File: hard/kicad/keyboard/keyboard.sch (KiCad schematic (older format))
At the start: 91 parts, among them SW01 Space, SW02 <, SW04 Tab, SW08 º \\, SW101 Space, SW11 Z, SW12 A, SW14 Q, SW18 1, SW1F1 Alt, SW1F2 Control, SW1F4 Shift, SW201 Space, SW21 X, SW22 S, SW24 W, SW28 2, SW31 C, SW32 D, SW34 E, SW38 3, SW41 V, SW42 F, SW44 R, SW48 4, SW51 B, SW52 G, SW54 T, SW58 5, SW61 N, SW62 H, SW64 Y, SW68 6, SW71 M, SW72 J, SW74 U, SW78 7, SW81 ,, SW82 K, SW84 I, SW88 8, SW91 ., SW92 L, SW94 O, SW98 9, U1 74HC154

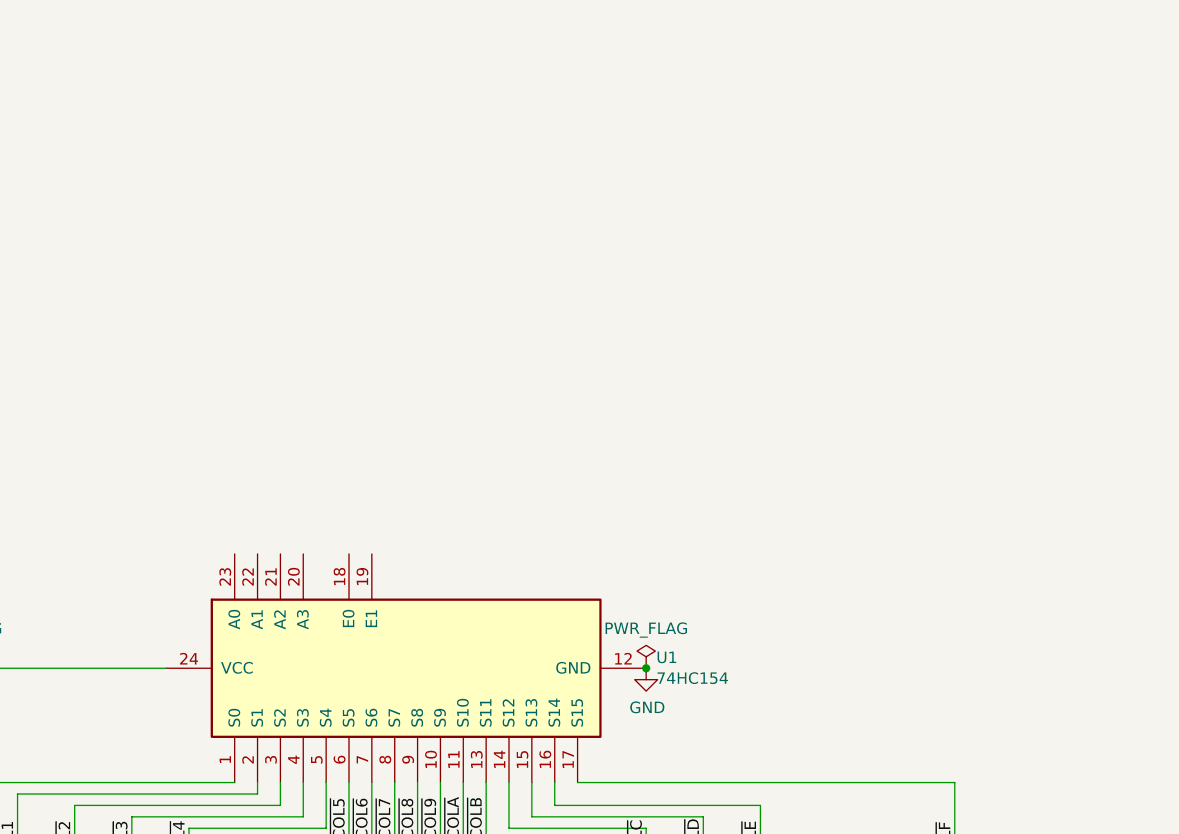
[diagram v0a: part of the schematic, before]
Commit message: update ASCII keyboard
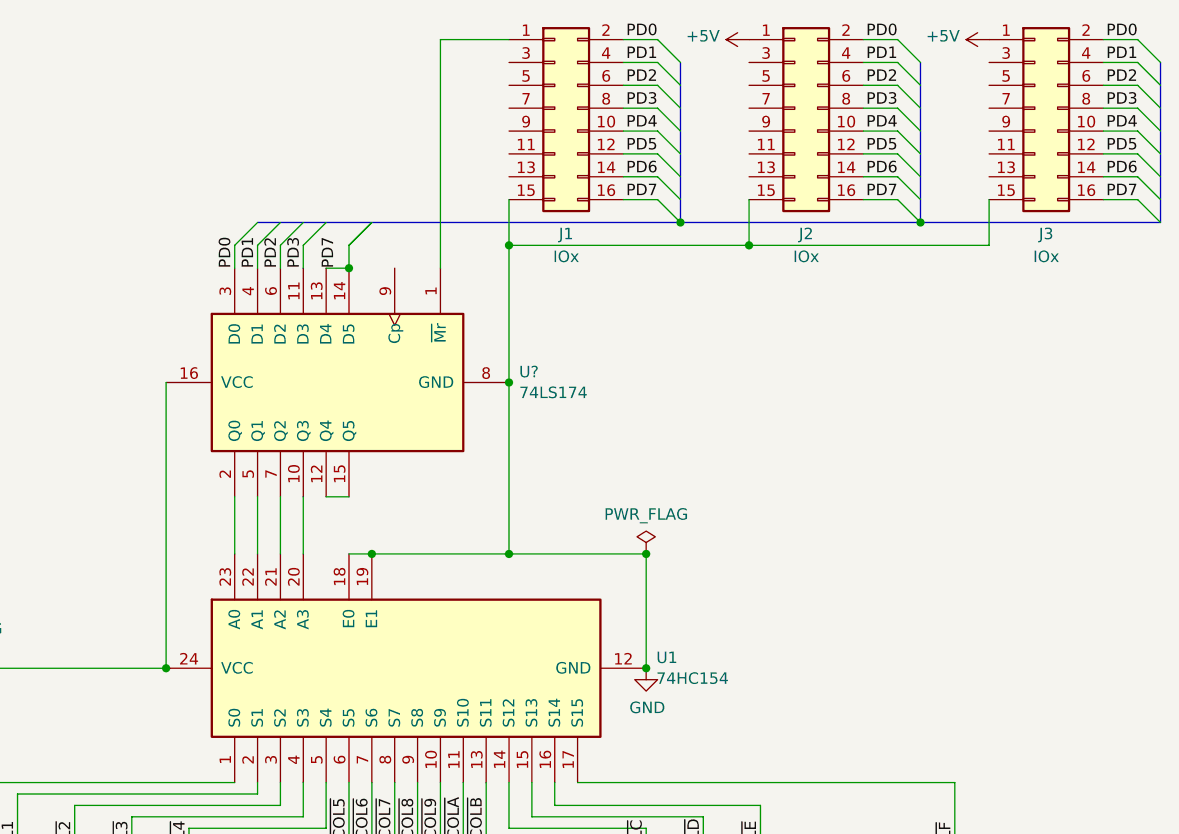
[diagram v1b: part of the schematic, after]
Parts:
- added J1, J2, J3: IOx, symbol Connector_Generic:Conn_02x08_Odd_Even
- added U?: 74LS174, symbol 74xx:74LS174
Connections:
- net +5V: now also J2.1 (Pin_1), J3.1 (Pin_1), U?.16 (VCC)
- net GND: now also U1.18 (E0), U1.19 (E1), J1.15 (Pin_15), J2.15 (Pin_15), J3.15 (Pin_15), U?.8 (GND)
- net at U1.20 (A3): now also U?.10 (Q3)
- net at U1.21 (A2): now also U?.7 (Q2)
- net at U1.22 (A1): now also U?.5 (Q1)
- net at U1.23 (A0): now also U?.2 (Q0)
- new net: J1.1 (Pin_1), U?.1 (~Mr)
- new net: U?.12 (Q4), U?.15 (Q5)
- new net PD0: J1.2 (Pin_2), J2.2 (Pin_2), J3.2 (Pin_2), U?.3 (D0)
- new net PD1: J1.4 (Pin_4), J2.4 (Pin_4), J3.4 (Pin_4), U?.4 (D1)
- new net PD2: J1.6 (Pin_6), J2.6 (Pin_6), J3.6 (Pin_6), U?.6 (D2)
- new net PD3: J1.8 (Pin_8), J2.8 (Pin_8), J3.8 (Pin_8), U?.11 (D3)
- new net PD4: J1.10 (Pin_10), J2.10 (Pin_10), J3.10 (Pin_10)
- new net PD5: J1.12 (Pin_12), J2.12 (Pin_12), J3.12 (Pin_12)
- new net PD6: J1.14 (Pin_14), J2.14 (Pin_14), J3.14 (Pin_14)
- new net PD7: J1.16 (Pin_16), J2.16 (Pin_16), J3.16 (Pin_16), U?.13 (D4), U?.14 (D5)

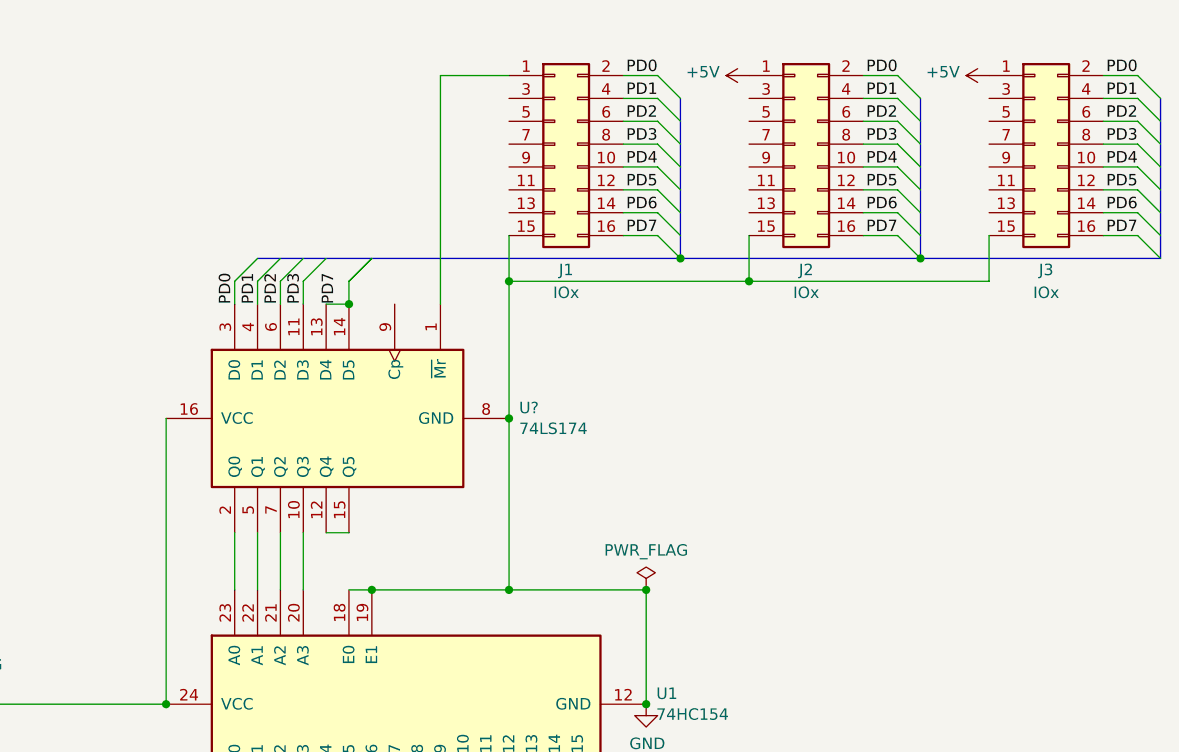
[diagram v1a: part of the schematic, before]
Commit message: more wiring on keyboard
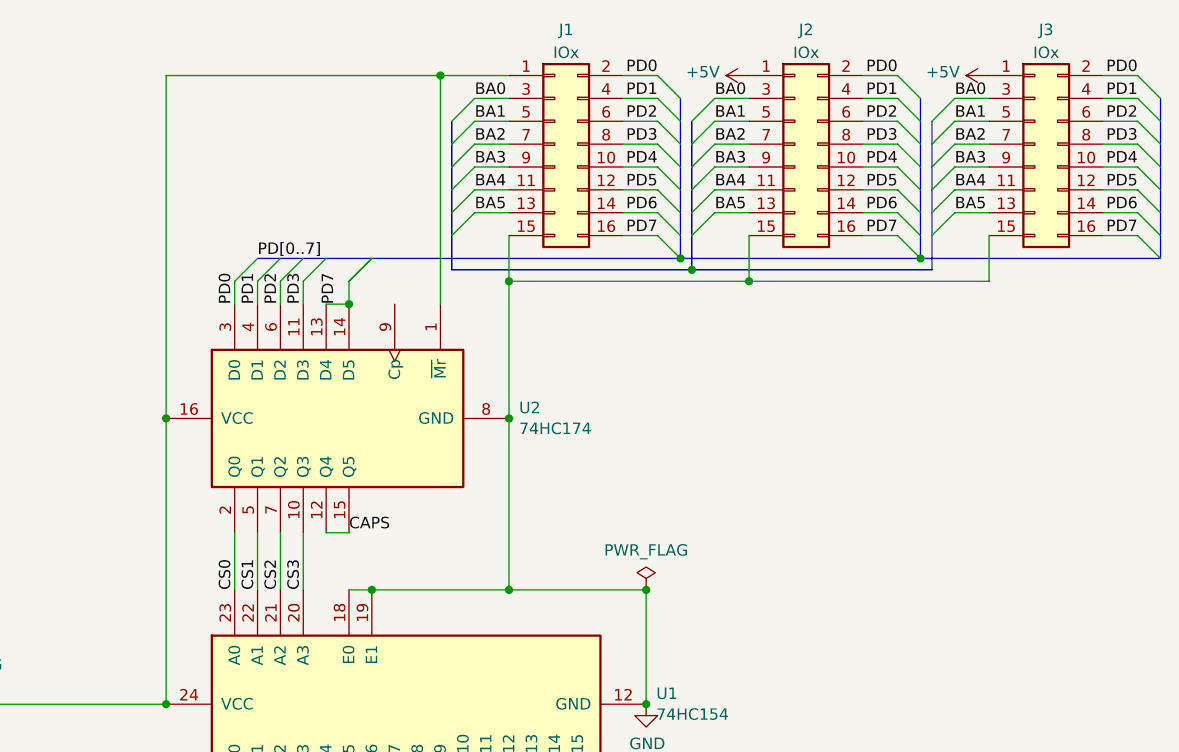
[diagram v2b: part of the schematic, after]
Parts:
- U2: renamed from U?; value 74LS174 -> 74HC174
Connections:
- net +5V: now also J1.1 (Pin_1), U2.1 (~Mr)
- net CS3: now reaches U1.20 (A3), U2.10 (Q3)
- net CAPS: now reaches U2.12 (Q4), U2.15 (Q5)
- net CS0: now reaches U1.23 (A0), U2.2 (Q0)
- net CS1: now reaches U1.22 (A1), U2.5 (Q1)
- net CS2: now reaches U1.21 (A2), U2.7 (Q2)
- net BA4: now reaches J1.11 (Pin_11)
- net BA4: now also J2.11 (Pin_11), J3.11 (Pin_11)
- net BA5: now reaches J1.13 (Pin_13)
- net BA5: now also J2.13 (Pin_13), J3.13 (Pin_13)
- net BA0: now reaches J1.3 (Pin_3)
- net BA0: now also J2.3 (Pin_3), J3.3 (Pin_3)
- net BA1: now reaches J1.5 (Pin_5)
- net BA1: now also J2.5 (Pin_5), J3.5 (Pin_5)
- net BA2: now reaches J1.7 (Pin_7)
- net BA2: now also J2.7 (Pin_7), J3.7 (Pin_7)
- net BA3: now reaches J1.9 (Pin_9)
- net BA3: now also J2.9 (Pin_9), J3.9 (Pin_9)
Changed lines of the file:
@@
 Connection ~ 4600 3250
 $Comp
-L 74xx:74LS174 U?
+L 74xx:74LS174 U2
 U 1 1 62809879
 P 3200 2500
-F 0 "U?" V 3154 1656 50  0000 R CNN
-F 1 "74LS174" V 3245 1656 50  0000 R CNN
+F 0 "U2" V 3154 1656 50  0000 R CNN
+F 1 "74HC174" V 3245 1656 50  0000 R CNN
 F 2 "" H 3200 2500 50  0001 C CNN
 F 3 "http://www.ti.com/lit/gpn/sn74LS174" H 3200 2500 50  0001 C CNN
@@
 U 1 1 628A1D51
 P 4200 1300
-F 0 "J1" H 4250 750 50  0000 C CNN
-F 1 "IOx" H 4250 650 50  0000 C CNN
+F 0 "J1" H 4250 1800 50  0000 C CNN
+F 1 "IOx" H 4250 1700 50  0000 C CNN
 F 2 "" H 4200 1300 50  0001 C CNN
 F 3 "~" H 4200 1300 50  0001 C CNN
@@
 U 1 1 628A4791
 P 5250 1300
-F 0 "J2" H 5300 750 50  0000 C CNN
-F 1 "IOx" H 5300 650 50  0000 C CNN
+F 0 "J2" H 5300 1800 50  0000 C CNN
+F 1 "IOx" H 5300 1700 50  0000 C CNN
 F 2 "" H 5250 1300 50  0001 C CNN
 F 3 "~" H 5250 1300 50  0001 C CNN
@@
 U 1 1 628A52CA
 P 6300 1300
-F 0 "J3" H 6350 750 50  0000 C CNN
-F 1 "IOx" H 6350 650 50  0000 C CNN
+F 0 "J3" H 6350 1800 50  0000 C CNN
+F 1 "IOx" H 6350 1700 50  0000 C CNN
 F 2 "" H 6300 1300 50  0001 C CNN
 F 3 "~" H 6300 1300 50  0001 C CNN
@@
 	4000 3250 4600 3250
 $Comp
-L power:+5V #PWR?
+L power:+5V #PWR0103
 U 1 1 629F2F72
 P 5050 1000
-F 0 "#PWR?" H 5050 850 50  0001 C CNN
+F 0 "#PWR0103" H 5050 850 50  0001 C CNN
 F 1 "+5V" V 5065 1128 50  0000 L CNN
 F 2 "" H 5050 1000 50  0001 C CNN
@@
 $EndComp
 $Comp
-L power:+5V #PWR?
+L power:+5V #PWR0104
 U 1 1 629F3068
 P 6100 1000
-F 0 "#PWR?" H 6100 850 50  0001 C CNN
+F 0 "#PWR0104" H 6100 850 50  0001 C CNN
 F 1 "+5V" V 6115 1128 50  0000 L CNN
 F 2 "" H 6100 1000 50  0001 C CNN
@@
 	6100 1900 6100 1700
 Connection ~ 5050 1900
+Text Label 2900 1800 0    50   ~ 0
+PD[0..7]
+Entry Wire Line
+	3750 1200 3850 1100
+Entry Wire Line
+	3750 1300 3850 1200
+Entry Wire Line
+	3750 1400 3850 1300
+Entry Wire Line
+	3750 1500 3850 1400
+Wire Wire Line
+	3850 1100 4000 1100
+Wire Wire Line
+	3850 1200 4000 1200
+Wire Wire Line
+	3850 1300 4000 1300
+Wire Wire Line
+	3850 1400 4000 1400
+Entry Wire Line
+	3750 1600 3850 1500
+Entry Wire Line
+	3750 1700 3850 1600
+Wire Wire Line
+	3850 1500 4000 1500
+Wire Wire Line
+	3850 1600 4000 1600
+Text Label 3850 1100 0    50   ~ 0
+BA0
+Text Label 3850 1200 0    50   ~ 0
+BA1
+Text Label 3850 1300 0    50   ~ 0
+BA2
+Text Label 3850 1400 0    50   ~ 0
+BA3
+Text Label 3850 1500 0    50   ~ 0
+BA4
+Text Label 3850 1600 0    50   ~ 0
+BA5
+Entry Wire Line
+	4800 1200 4900 1100
+Entry Wire Line
+	4800 1300 4900 1200
+Entry Wire Line
+	4800 1400 4900 1300
+Entry Wire Line
+	4800 1500 4900 1400
+Wire Wire Line
+	4900 1100 5050 1100
+Wire Wire Line
+	4900 1200 5050 1200
+Wire Wire Line
+	4900 1300 5050 1300
+Wire Wire Line
+	4900 1400 5050 1400
+Entry Wire Line
+	4800 1600 4900 1500
+Entry Wire Line
+	4800 1700 4900 1600
+Wire Wire Line
+	4900 1500 5050 1500
+Wire Wire Line
+	4900 1600 5050 1600
+Text Label 4900 1100 0    50   ~ 0
+BA0
+Text Label 4900 1200 0    50   ~ 0
+BA1
+Text Label 4900 1300 0    50   ~ 0
+BA2
+Text Label 4900 1400 0    50   ~ 0
+BA3
+Text Label 4900 1500 0    50   ~ 0
+BA4
+Text Label 4900 1600 0    50   ~ 0
+BA5
+Entry Wire Line
+	5850 1200 5950 1100
+Entry Wire Line
+	5850 1300 5950 1200
+Entry Wire Line
+	5850 1400 5950 1300
+Entry Wire Line
+	5850 1500 5950 1400
+Wire Wire Line
+	5950 1100 6100 1100
+Wire Wire Line
+	5950 1200 6100 1200
+Wire Wire Line
+	5950 1300 6100 1300
+Wire Wire Line
+	5950 1400 6100 1400
+Entry Wire Line
+	5850 1600 5950 1500
+Entry Wire Line
+	5850 1700 5950 1600
+Wire Wire Line
+	5950 1500 6100 1500
+Wire Wire Line
+	5950 1600 6100 1600
+Text Label 5950 1100 0    50   ~ 0
+BA0
+Text Label 5950 1200 0    50   ~ 0
+BA1
+Text Label 5950 1300 0    50   ~ 0
+BA2
+Text Label 5950 1400 0    50   ~ 0
+BA3
+Text Label 5950 1500 0    50   ~ 0
+BA4
+Text Label 5950 1600 0    50   ~ 0
+BA5
+Wire Bus Line
+	3750 1850 4800 1850
+Wire Bus Line
+	4800 1850 5850 1850
+Connection ~ 4800 1850
+Text Label 2800 3250 1    50   ~ 0
+CS0
+Text Label 2900 3250 1    50   ~ 0
+CS1
+Text Label 3000 3250 1    50   ~ 0
+CS2
+Text Label 3100 3250 1    50   ~ 0
+CS3
+Wire Wire Line
+	3700 1000 2500 1000
+Wire Wire Line
+	2500 1000 2500 2500
 Wire Bus Line
 	2900 1800 4750 1800
@@
 Wire Bus Line
 	4750 1100 4750 1800
+Wire Bus Line
+	3750 1200 3750 1850
+Wire Bus Line
+	4800 1200 4800 1850
+Wire Bus Line
+	5850 1200 5850 1850
+Connection ~ 3700 1000
+Connection ~ 2500 2500
+Text Label 3300 3000 0    50   ~ 0
+CAPS
 $EndSCHEMATC
